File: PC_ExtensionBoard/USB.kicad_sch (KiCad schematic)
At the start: 84 parts, among them U1 HC-USB3.0-L168-WP, U10 AP22615A_TSOT26, U11 ALC662, U13 AP22615A_TSOT26, U14 ESD204DQAR, U15 AP22615A_TSOT26, U16 ESD204DQAR, U17 AP22615A_TSOT26, U18 ESD204DQAR, U22 ESD204DQAR, U7 HC-USB3.0-L168-WP, U8 ESD204DQAR

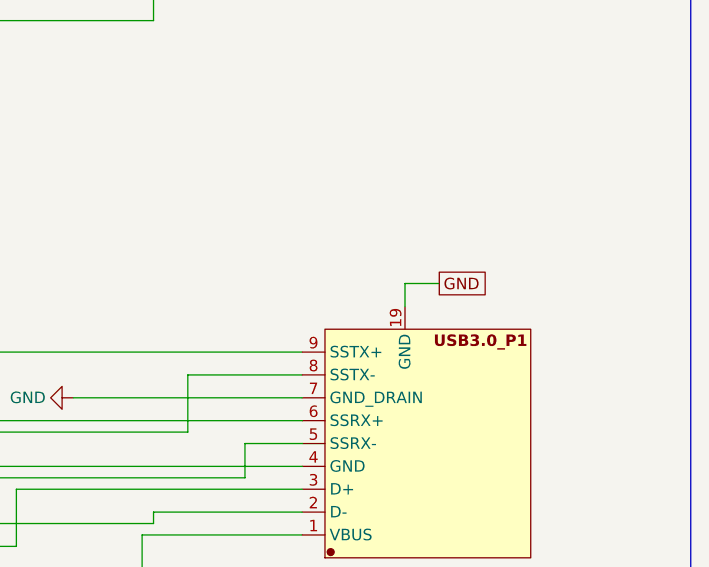
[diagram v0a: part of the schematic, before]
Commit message: finished highspeed routing
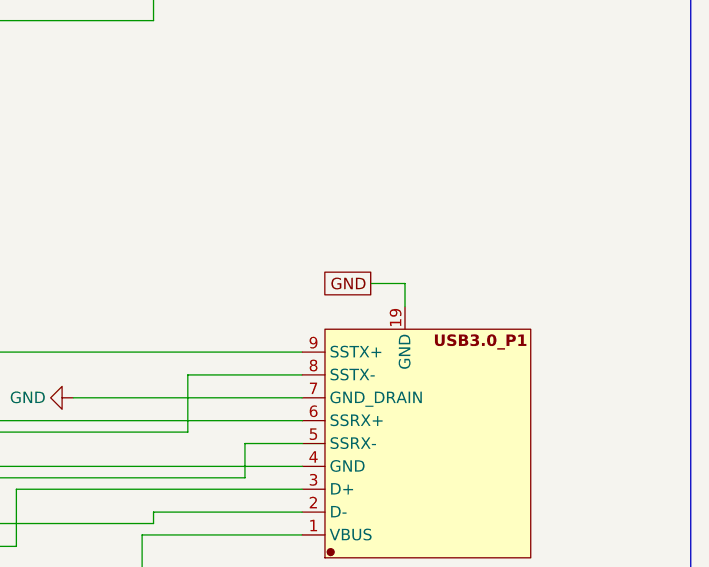
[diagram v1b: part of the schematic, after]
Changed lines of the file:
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@@
 	(wire
 		(pts
-			(xy 796.29 100.33) (xy 800.1 100.33)
+			(xy 796.29 100.33) (xy 792.48 100.33)
 		)
 		(stroke
@@
 	(global_label "GND"
 		(shape passive)
-		(at 800.1 100.33 0)
+		(at 792.48 100.33 180)
 		(fields_autoplaced yes)
 		(effects
@@
 				(size 1.27 1.27)
 			)
-			(justify left)
+			(justify right)
 		)
 		(property "Intersheetrefs" "${INTERSHEET_REFS}"
-			(at 805.8444 100.33 0)
+			(at 786.7356 100.33 0)
 			(hide yes)
 			(show_name no)
@@
 					(size 1.27 1.27)
 				)
-				(justify left)
-			)
-		)
+				(justify right)
+			)
+		)
